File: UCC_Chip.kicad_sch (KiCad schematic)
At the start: 12 parts, among them U1 BQ25173DSG, U2 LM1881

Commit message: j
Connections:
- net Chip_In renamed Chip_Out
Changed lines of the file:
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@@
 	(wire
 		(pts
-			(xy 68.58 86.36) (xy 99.06 86.36)
+			(xy 68.58 86.36) (xy 100.33 86.36)
 		)
 		(stroke
@@
 		)
 	)
-	(hierarchical_label "Chip_In"
+	(hierarchical_label "Chip_Out"
 		(shape input)
 		(at 34.29 53.34 180)

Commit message: Added sheet pins
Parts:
- removed U1: BQ25173DSG, Package_SON:Texas_DSG0008A_WSON-8-1EP_2x2mm_P0.5mm_EP0.9x1.6mm, symbol Battery_Management:BQ25173DSG
- removed U2: LM1881, RF_GSM:Quectel_BG95, symbol Video:LM1881
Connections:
- net Chip_Out renamed Zener_UCC_Chip
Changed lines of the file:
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@@
 		)
 	)
-	(hierarchical_label "Chip_Out"
+	(hierarchical_label "Rectifier_UCC_In"
+		(shape input)
+		(at 121.92 45.72 0)
+		(effects
+			(font
+				(size 1.27 1.27)
+			)
+			(justify left)
+		)
+	)
+	(hierarchical_label "Zener_UCC_Chip"
 		(shape input)
 		(at 34.29 53.34 180)
@@
 	)
 	(symbol
-		(lib_id "Video:LM1881")
-		(at 176.53 68.58 0)
-		(unit 1)
-		(body_style 1)
-		(exclude_from_sim no)
-		(in_bom yes)
-		(on_board yes)
-		(in_pos_files yes)
-		(dnp no)
-		(fields_autoplaced yes)
-		(property "Reference" "U2"
-			(at 178.6733 55.88 0)
-			(show_name no)
-			(do_not_autoplace no)
-			(effects
-				(font
-					(size 1.27 1.27)
-				)
-				(justify left)
-			)
-		)
-		(property "Value" "LM1881"
-			(at 178.6733 58.42 0)
-			(show_name no)
-			(do_not_autoplace no)
-			(effects
-				(font
-					(size 1.27 1.27)
-				)
-				(justify left)
-			)
-		)
-		(property "Footprint" "RF_GSM:Quectel_BG95"
-			(at 176.53 84.582 0)
-			(hide yes)
-			(show_name no)
-			(do_not_autoplace no)
-			(effects
-				(font
-					(size 1.27 1.27)
-				)
-			)
-		)
-		(property "Datasheet" "https://www.ti.com/lit/ds/symlink/lm1881.pdf"
-			(at 176.53 82.296 0)
-			(hide yes)
-			(show_name no)
-			(do_not_autoplace no)
-			(effects
-				(font
-					(size 1.27 1.27)
-				)
-			)
-		)
-		(property "Description" "Video Sync Separator, composite sync and vertical sync outputs, DIP-8 / SOIC-8"
-			(at 176.53 80.01 0)
-			(hide yes)
-			(show_name no)
-			(do_not_autoplace no)
-			(effects
-				(font
-					(size 1.27 1.27)
-				)
-			)
-		)
-		(pin "5"
-		)
-		(pin "4"
-		)
-		(pin "3"
-		)
-		(pin "2"
-		)
-		(pin "1"
-		)
-		(pin "7"
-		)
-		(pin "6"
-		)
-		(pin "8"
-		)
-		(instances
-			(project "Solar_Battery"
-				(path "/6805959e-39bb-4644-b93e-3970e29fedc0/a320594e-eb17-43a9-8193-2f75b3718179/23661c41-dbb5-4ca2-a742-531e78ada01c"
-					(reference "U2")
-					(unit 1)
-				)
-			)
-		)
-	)
-	(symbol
 		(lib_id "Diode:1N914")
 		(at 68.58 53.34 180)
@@
 					(unit 1)
 				)
-			)
-		)
-	)
-	(symbol
-		(lib_id "Battery_Management:BQ25173DSG")
-		(at 113.03 85.09 0)
-		(unit 1)
-		(body_style 1)
-		(exclude_from_sim no)
-		(in_bom yes)
-		(on_board yes)
-		(in_pos_files yes)
-		(dnp no)
-		(fields_autoplaced yes)
-		(property "Reference" "U1"
-			(at 113.03 72.39 0)
-			(show_name no)
-			(do_not_autoplace no)
-			(effects
-				(font
-					(size 1.27 1.27)
-				)
-			)
-		)
-		(property "Value" "BQ25173DSG"
-			(at 113.03 74.93 0)
-			(show_name no)
-			(do_not_autoplace no)
-			(effects
-				(font
-					(size 1.27 1.27)
-				)
-			)
-		)
-		(property "Footprint" "Package_SON:Texas_DSG0008A_WSON-8-1EP_2x2mm_P0.5mm_EP0.9x1.6mm"
-			(at 142.24 93.98 0)
-			(hide yes)
-			(show_name no)
-			(do_not_autoplace no)
-			(effects
-				(font
-					(size 1.27 1.27)
-				)
-			)
-		)
-		(property "Datasheet" "https://www.ti.com/lit/ds/symlink/bq25173.pdf"
-			(at 113.03 85.09 0)
-			(hide yes)
-			(show_name no)
-			(do_not_autoplace no)
-			(effects
-				(font
-					(size 1.27 1.27)
-				)
-			)
-		)
-		(property "Description" "800-mA Linear Charger for 1- to 4-Cell Supercapacitor, input 3 to 18v, WSON-8"
-			(at 113.03 85.09 0)
-			(hide yes)
-			(show_name no)
-			(do_not_autoplace no)
-			(effects
-				(font
-					(size 1.27 1.27)
-				)
-			)
-		)
-		(pin "9"
-		)
-		(pin "8"
-		)
-		(pin "7"
-		)
-		(pin "3"
-		)
-		(pin "1"
-		)
-		(pin "5"
-		)
-		(pin "2"
-		)
-		(pin "4"
-		)
-		(pin "6"
-		)
-		(instances
-			(project "Solar_Battery"
-				(path "/6805959e-39bb-4644-b93e-3970e29fedc0/a320594e-eb17-43a9-8193-2f75b3718179/23661c41-dbb5-4ca2-a742-531e78ada01c"
-					(reference "U1")
-					(unit 1)
-				)

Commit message: something
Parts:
- added ucc_1: (no value), symbol UCC28710:ucc_chip
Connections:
- net at +.1 (K), +.2, CDD.1: now also ucc_1.1 (VDD)
- net at +.1, +.2: now also ucc_1.2 (VS)
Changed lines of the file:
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@@
+	(wire
+		(pts
+			(xy 95.25 74.93) (xy 100.33 74.93)
+		)
+		(stroke
+			(width 0)
+			(type default)
+		)
+	)
 	(wire
 		(pts
@@
 	(wire
 		(pts
+			(xy 96.52 77.47) (xy 100.33 77.47)
+		)
+		(stroke
+			(width 0)
+			(type default)
+		)
+	)
+	(wire
+		(pts
+			(xy 95.25 83.82) (xy 95.25 74.93)
+		)
+		(stroke
+			(width 0)
+			(type default)
+		)
+	)
+	(wire
+		(pts
 			(xy 91.44 99.06) (xy 87.63 99.06)
 		)
@@
 	(wire
 		(pts
-			(xy 68.58 86.36) (xy 100.33 86.36)
-		)
-		(stroke
-			(width 0)
-			(type default)
-		)
-	)
-	(wire
-		(pts
 			(xy 91.44 71.12) (xy 91.44 77.47)
 		)
@@
 	(wire
 		(pts
-			(xy 81.28 83.82) (xy 99.06 83.82)
-		)
-		(stroke
-			(width 0)
-			(type default)
-		)
-	)
-	(wire
-		(pts
 			(xy 124.46 88.9) (xy 127 88.9)
 		)
@@
 	(wire
 		(pts
+			(xy 96.52 86.36) (xy 96.52 77.47)
+		)
+		(stroke
+			(width 0)
+			(type default)
+		)
+	)
+	(wire
+		(pts
 			(xy 60.96 88.9) (xy 60.96 93.98)
 		)
@@
 	(wire
 		(pts
+			(xy 68.58 86.36) (xy 96.52 86.36)
+		)
+		(stroke
+			(width 0)
+			(type default)
+		)
+	)
+	(wire
+		(pts
 			(xy 58.42 53.34) (xy 64.77 53.34)
 		)
@@
 		(pts
 			(xy 179.07 78.74) (xy 184.15 78.74)
+		)
+		(stroke
+			(width 0)
+			(type default)
+		)
+	)
+	(wire
+		(pts
+			(xy 81.28 83.82) (xy 95.25 83.82)
 		)
 		(stroke
@@
 		)
 		(instances
+			(project "UCC_Chip"
+				(path "/33cfd970-7195-40cd-87dc-a099d1f2e89f"
+					(reference "+")
+					(unit 1)
+				)
+			)
 			(project "Solar_Battery"
 				(path "/6805959e-39bb-4644-b93e-3970e29fedc0/a320594e-eb17-43a9-8193-2f75b3718179/23661c41-dbb5-4ca2-a742-531e78ada01c"
@@
 		)
 		(instances
+			(project "UCC_Chip"
+				(path "/33cfd970-7195-40cd-87dc-a099d1f2e89f"
+					(reference "+")
+					(unit 1)
+				)
+			)
 			(project "Solar_Battery"
 				(path "/6805959e-39bb-4644-b93e-3970e29fedc0/a320594e-eb17-43a9-8193-2f75b3718179/23661c41-dbb5-4ca2-a742-531e78ada01c"
@@
 		)
 		(instances
+			(project "UCC_Chip"
+				(path "/33cfd970-7195-40cd-87dc-a099d1f2e89f"
+					(reference "+")
+					(unit 1)
+				)
+			)
 			(project "Solar_Battery"
 				(path "/6805959e-39bb-4644-b93e-3970e29fedc0/a320594e-eb17-43a9-8193-2f75b3718179/23661c41-dbb5-4ca2-a742-531e78ada01c"
@@
 		)
 		(instances
+			(project "UCC_Chip"
+				(path "/33cfd970-7195-40cd-87dc-a099d1f2e89f"
+					(reference "+")
+					(unit 1)
+				)
+			)
 			(project "Solar_Battery"
 				(path "/6805959e-39bb-4644-b93e-3970e29fedc0/a320594e-eb17-43a9-8193-2f75b3718179/23661c41-dbb5-4ca2-a742-531e78ada01c"
 					(reference "+")
+					(unit 1)
+				)
+			)
+		)
+	)
+	(symbol
+		(lib_id "UCC28710:ucc_chip")
+		(at 113.03 78.74 0)
+		(unit 1)
+		(body_style 1)
+		(exclude_from_sim no)
+		(in_bom yes)
+		(on_board yes)
+		(in_pos_files yes)
+		(dnp no)
+		(fields_autoplaced yes)
+		(property "Reference" "ucc_1"
+			(at 113.03 68.58 0)
+			(show_name no)
+			(do_not_autoplace no)
+			(effects
+				(font
+					(size 1.27 1.27)
+				)
+			)
+		)
+		(property "Value" ""
+			(at 113.03 78.74 0)
+			(show_name no)
+			(do_not_autoplace no)
+			(effects
+				(font
+					(size 1.27 1.27)
+				)
+			)
+		)
+		(property "Footprint" ""
+			(at 113.03 78.74 0)
+			(hide yes)
+			(show_name no)
+			(do_not_autoplace no)
+			(effects
+				(font
+					(size 1.27 1.27)
+				)
+			)
+		)
+		(property "Datasheet" ""
+			(at 113.03 78.74 0)
+			(hide yes)
+			(show_name no)
+			(do_not_autoplace no)
+			(effects
+				(font
+					(size 1.27 1.27)
+				)
+			)
+		)
+		(property "Description" ""
+			(at 113.03 78.74 0)
+			(hide yes)
+			(show_name no)
+			(do_not_autoplace no)
+			(effects
+				(font
+					(size 1.27 1.27)
+				)
+			)
+		)
+		(pin "1"
+		)
+		(pin "6"
+		)
+		(pin "8"
+		)
+		(pin "2"
+		)
+		(pin "4"
+		)
+		(pin "5"
+		)
+		(pin "3"
+		)
+		(instances
+			(project "UCC_Chip"
+				(path "/33cfd970-7195-40cd-87dc-a099d1f2e89f"
+					(reference "ucc_1")
 					(unit 1)
 				)
@@
 		)
 		(instances
+			(project "UCC_Chip"
+				(path "/33cfd970-7195-40cd-87dc-a099d1f2e89f"
+					(reference "#PWR05")
+					(unit 1)
+				)
+			)
 			(project "Solar_Battery"
 				(path "/6805959e-39bb-4644-b93e-3970e29fedc0/a320594e-eb17-43a9-8193-2f75b3718179/23661c41-dbb5-4ca2-a742-531e78ada01c"
@@
 		)
 		(instances
+			(project "UCC_Chip"
+				(path "/33cfd970-7195-40cd-87dc-a099d1f2e89f"
+					(reference "+")
+					(unit 1)
+				)
+			)
 			(project "Solar_Battery"
 				(path "/6805959e-39bb-4644-b93e-3970e29fedc0/a320594e-eb17-43a9-8193-2f75b3718179/23661c41-dbb5-4ca2-a742-531e78ada01c"
@@
 		)
 		(instances
+			(project "UCC_Chip"
+				(path "/33cfd970-7195-40cd-87dc-a099d1f2e89f"
+					(reference "+")
+					(unit 1)
+				)
+			)
 			(project "Solar_Battery"
 				(path "/6805959e-39bb-4644-b93e-3970e29fedc0/a320594e-eb17-43a9-8193-2f75b3718179/23661c41-dbb5-4ca2-a742-531e78ada01c"
@@
 		)
 		(instances
+			(project "UCC_Chip"
+				(path "/33cfd970-7195-40cd-87dc-a099d1f2e89f"
+					(reference "+")
+					(unit 1)
+				)
+			)
 			(project "Solar_Battery"
 				(path "/6805959e-39bb-4644-b93e-3970e29fedc0/a320594e-eb17-43a9-8193-2f75b3718179/23661c41-dbb5-4ca2-a742-531e78ada01c"
@@
 		)
 		(instances
+			(project "UCC_Chip"
+				(path "/33cfd970-7195-40cd-87dc-a099d1f2e89f"
+					(reference "#PWR02")
+					(unit 1)
+				)
+			)
 			(project "Solar_Battery"
 				(path "/6805959e-39bb-4644-b93e-3970e29fedc0/a320594e-eb17-43a9-8193-2f75b3718179/23661c41-dbb5-4ca2-a742-531e78ada01c"
@@
 		)
 		(instances
+			(project "UCC_Chip"
+				(path "/33cfd970-7195-40cd-87dc-a099d1f2e89f"
+					(reference "+")
+					(unit 1)
+				)
+			)
 			(project "Solar_Battery"
 				(path "/6805959e-39bb-4644-b93e-3970e29fedc0/a320594e-eb17-43a9-8193-2f75b3718179/23661c41-dbb5-4ca2-a742-531e78ada01c"
@@
 		)
 		(instances
+			(project "UCC_Chip"
+				(path "/33cfd970-7195-40cd-87dc-a099d1f2e89f"
+					(reference "#PWR03")
+					(unit 1)
+				)
+			)
 			(project "Solar_Battery"
 				(path "/6805959e-39bb-4644-b93e-3970e29fedc0/a320594e-eb17-43a9-8193-2f75b3718179/23661c41-dbb5-4ca2-a742-531e78ada01c"
@@
 		)
 		(instances
+			(project "UCC_Chip"
+				(path "/33cfd970-7195-40cd-87dc-a099d1f2e89f"
+					(reference "CDD")
+					(unit 1)
+				)
+			)
 			(project "Solar_Battery"
 				(path "/6805959e-39bb-4644-b93e-3970e29fedc0/a320594e-eb17-43a9-8193-2f75b3718179/23661c41-dbb5-4ca2-a742-531e78ada01c"
@@
 		)
 		(instances
+			(project "UCC_Chip"
+				(path "/33cfd970-7195-40cd-87dc-a099d1f2e89f"
+					(reference "+")
+					(unit 1)
+				)
+			)
 			(project "Solar_Battery"
 				(path "/6805959e-39bb-4644-b93e-3970e29fedc0/a320594e-eb17-43a9-8193-2f75b3718179/23661c41-dbb5-4ca2-a742-531e78ada01c"
@@
 		)
 		(instances
+			(project "UCC_Chip"
+				(path "/33cfd970-7195-40cd-87dc-a099d1f2e89f"
+					(reference "#PWR04")
+					(unit 1)
+				)
+			)
 			(project "Solar_Battery"
 				(path "/6805959e-39bb-4644-b93e-3970e29fedc0/a320594e-eb17-43a9-8193-2f75b3718179/23661c41-dbb5-4ca2-a742-531e78ada01c"
@@
 		)
 	)
+	(sheet_instances
+		(path "/"
+			(page "1")
+		)
+	)
+	(embedded_fonts no)
 )

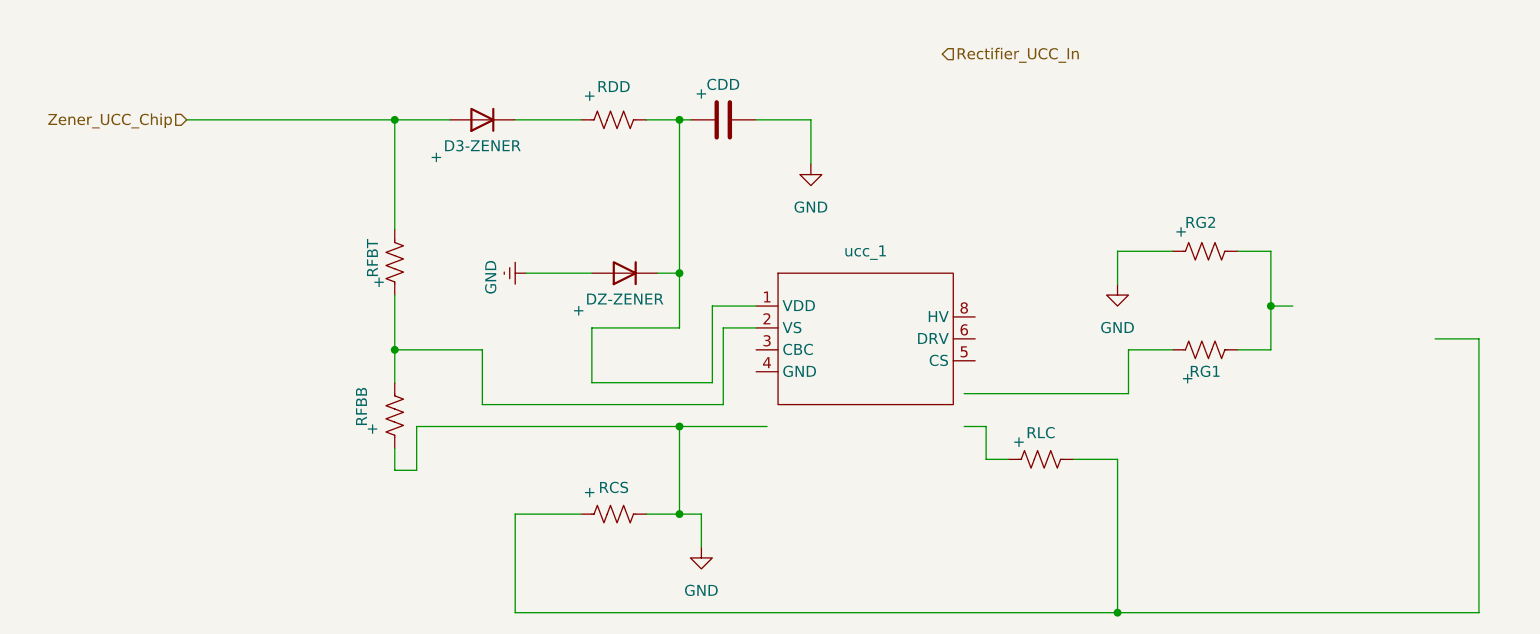
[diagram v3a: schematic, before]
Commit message: Added the ucc28710 symbol in the schematic and its footprint. Added the mosfet symbol. Connected the final missing connections in the schematics. annotated  it. if done right, only a few footprints need assignment in the uccchip subsheet
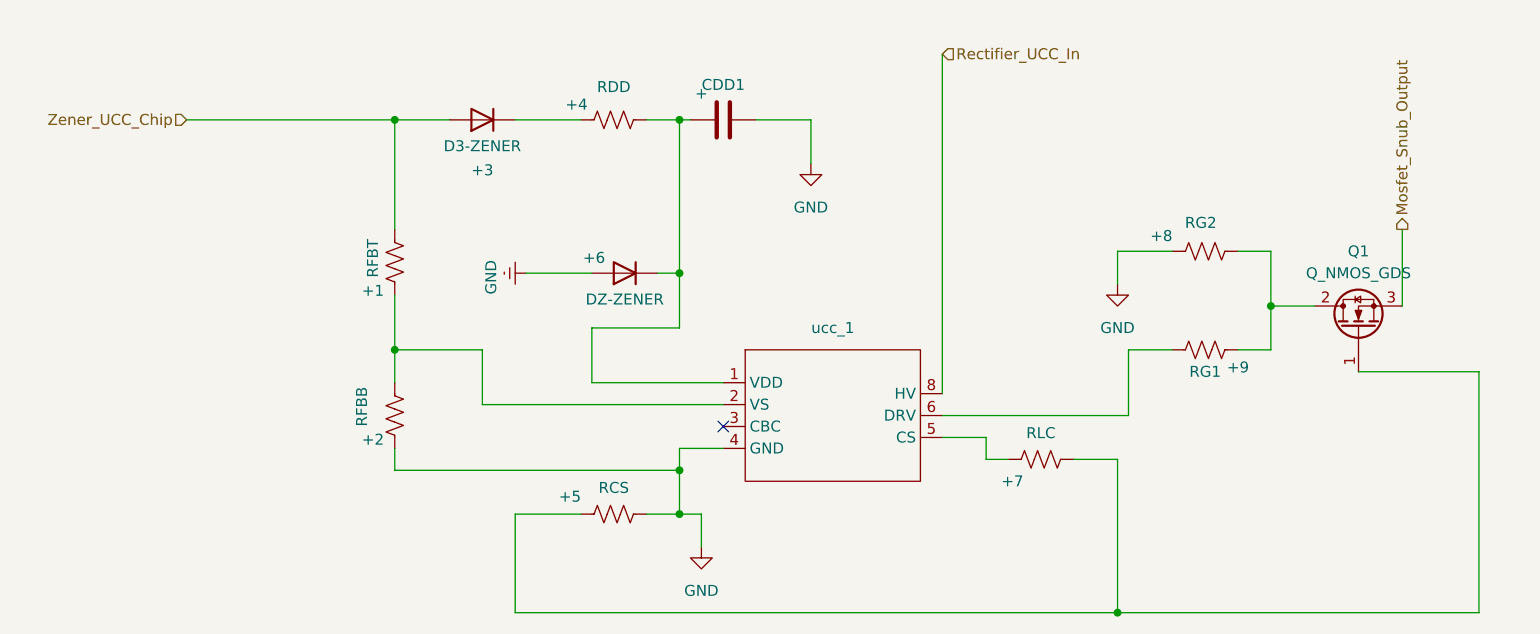
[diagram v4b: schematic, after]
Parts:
- added Q1: Q_NMOS_GDS, symbol Transistor_FET:Q_NMOS_GDS
- ucc_1: footprint (none) -> UCC28710_footprint:SO_UCC28710D_TEX
- renumbered + to +1, + to +2, + to +3, + to +4, + to +5, + to +6, + to +7, + to +8, + to +9, CDD to CDD1
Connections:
- net GND: now also ucc_1.4 (GND)
- net Rectifier_UCC_In: now also ucc_1.8 (HV)
- net at +5.1, +7.2: now also Q1.1 (G)
- net at ucc_1.5 (CS): now also +7.1
- net at ucc_1.6 (DRV): now also +9.1
- net at +8.2, +9.2: now also Q1.2 (D)
- new net Mosfet_Snub_Output: Q1.3 (S)
- no-connect marks 0 -> 1
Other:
- moved on the sheet: ucc_1
